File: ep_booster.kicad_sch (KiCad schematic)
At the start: 28 parts, among them J1 TB002-500-04BE, J2 Conn_01x04_Pin, Q1 MMBF5457, Q2 BC849C

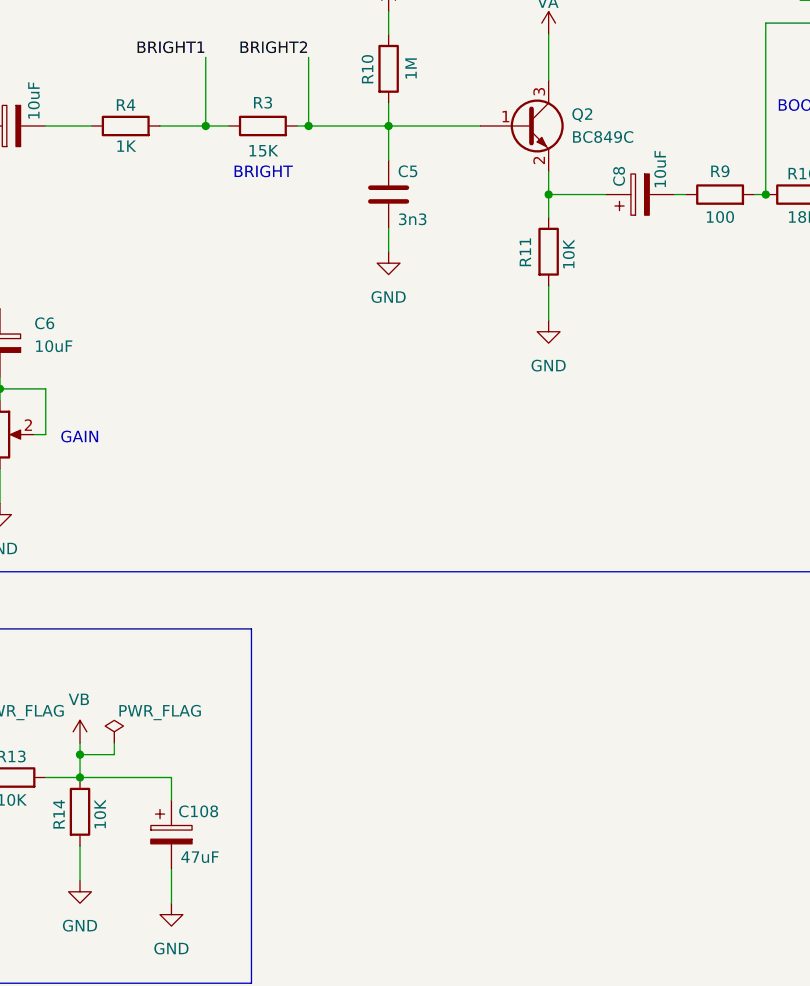
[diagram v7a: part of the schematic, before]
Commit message: add F.Silkscreen for IO, update C ref des
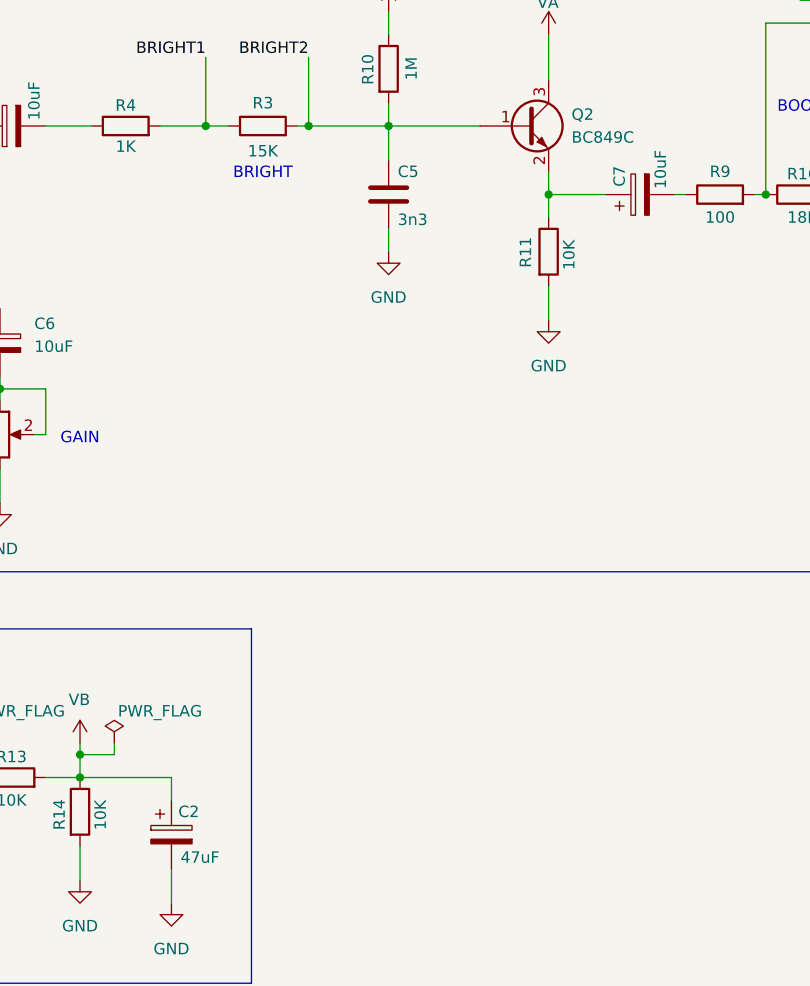
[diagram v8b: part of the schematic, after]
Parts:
- C5: footprint Capacitor_THT:C_Rect_L7.2mm_W2.5mm_P5.00mm_FKS2_FKP2_MKS2_MKP2 -> Capacitor_THT:C_Rect_L7.2mm_W3.0mm_P5.00mm_FKS2_FKP2_MKS2_MKP2
- renumbered C108 to C2, C8 to C7
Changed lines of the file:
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@@
 	(title_block
 		(title "EP Booster")
-		(date "2025-02-23")
+		(date "2025-02-27")
 		(rev "1.0.0")
 		(company "Miloš Garunović")
@@
 		(on_board yes)
 		(dnp no)
-		(property "Reference" "C8"
+		(property "Reference" "C7"
 			(at 151.384 50.038 0)
 			(effects
@@
 		)
 		(property "Description" "Polarized capacitor"
+			(at 153.67 52.07 0)
+			(effects
+				(font
+					(size 1.27 1.27)
+				)
+				(hide yes)
+			)
+		)
+		(property "Purpose" ""
 			(at 153.67 52.07 0)
 			(effects
@@
 			(project "ep_booster"
 				(path "/fa0b5818-9ee4-4073-a6e2-e7b6ccd60214"
-					(reference "C8")
+					(reference "C7")
 					(unit 1)
 				)
@@
 		(on_board yes)
 		(dnp no)
-		(property "Reference" "C108"
+		(property "Reference" "C2"
 			(at 102.362 120.65 0)
 			(effects
@@
 			(project "ep_booster"
 				(path "/fa0b5818-9ee4-4073-a6e2-e7b6ccd60214"
-					(reference "C108")
+					(reference "C2")
 					(unit 1)
 				)
@@
 			)
 		)
-		(property "Footprint" "Capacitor_THT:C_Rect_L7.2mm_W2.5mm_P5.00mm_FKS2_FKP2_MKS2_MKP2"
+		(property "Footprint" "Capacitor_THT:C_Rect_L7.2mm_W3.0mm_P5.00mm_FKS2_FKP2_MKS2_MKP2"
 			(at 126.6952 55.88 0)
 			(effects
@@
 			(at 125.73 52.07 0)
 			(effects
+				(font
+					(size 1.27 1.27)
+				)
+				(hide yes)
+			)
+		)
+		(property "Purpose" ""
+			(at 125.73 52.07 0)
+			(effects
